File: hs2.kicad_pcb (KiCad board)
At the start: 2 copper layers, 70 x 85 mm, 88 parts, among them J1 Conn_01x01, J2 Conn_01x01, J3 Conn_01x02, Q1 2N5457, Q2 2N3904, Q3 2N3906, Q4 2N3904, U1 Opamp_Dual, U2 Opamp_Dual, U3 Opamp_Dual

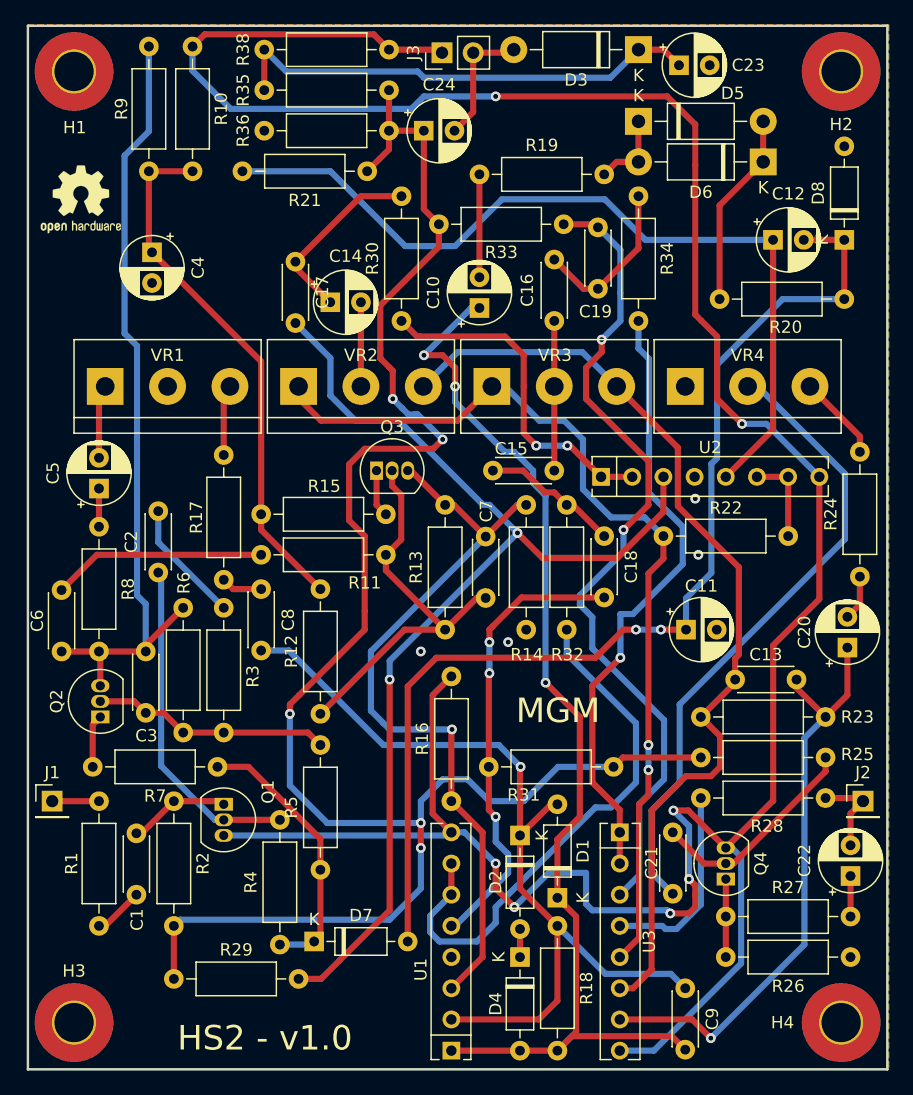
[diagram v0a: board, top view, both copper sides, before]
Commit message: layout: Fixing DRC warnings
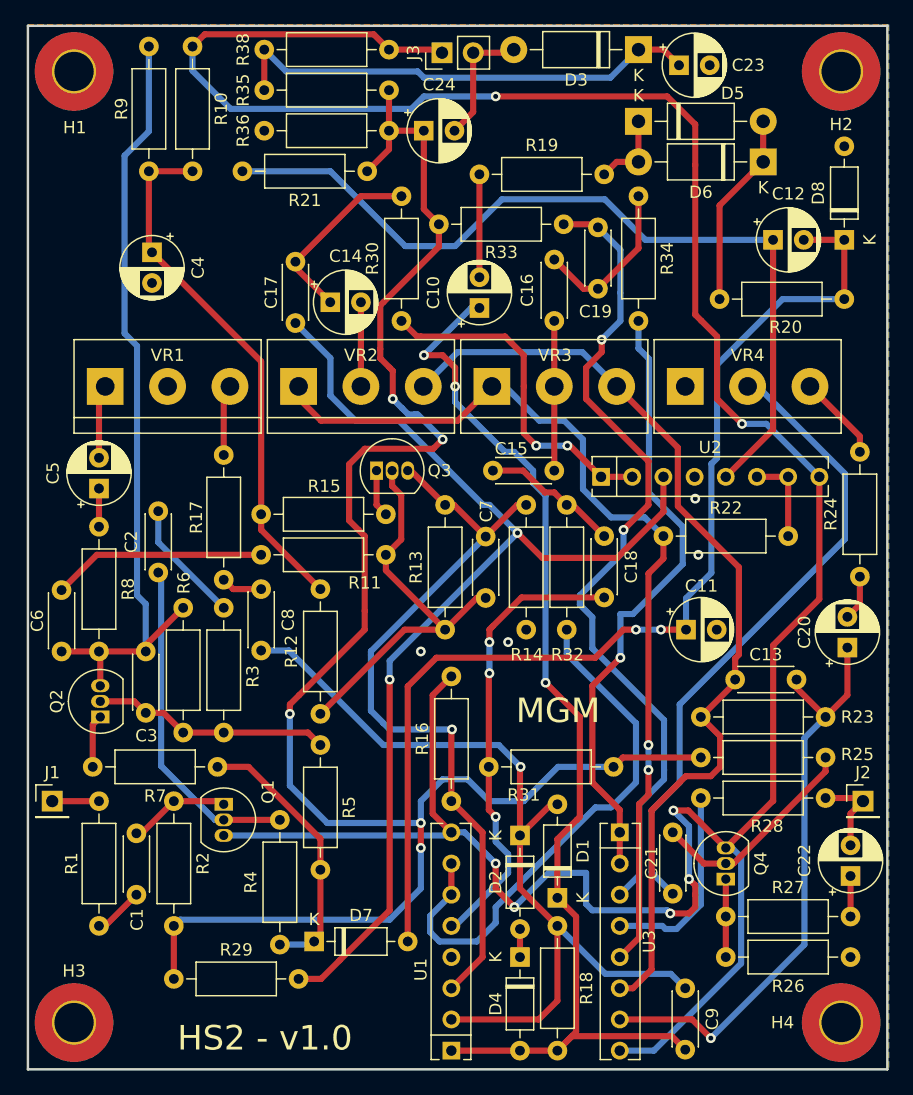
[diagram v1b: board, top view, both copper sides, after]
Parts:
- removed REF**: OSHW-Logo2_7.3x6mm_SilkScreen, Symbol:OSHW-Logo2_7.3x6mm_SilkScreen

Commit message: Minor improvements
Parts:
- added J4: Conn_01x01, Connector_PinHeader_2.54mm:PinHeader_1x01_P2.54mm_Vertical, F.Cu at (103.6, 124.5)
- added J5: Conn_01x01, Connector_PinHeader_2.54mm:PinHeader_1x01_P2.54mm_Vertical, F.Cu at (146.8, 59.2)
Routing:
- net +9V: track 232.0 -> 234.5 mm
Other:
- board text added: "1"
- board text added: "3"
- board text added: "HS2 v1.0"
- board text added: "Input"
- board text added: "Output"
- board text removed: "HS2 - v1.0"
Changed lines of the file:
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@@
     )
   )
+  (footprint "Connector_PinHeader_2.54mm:PinHeader_1x01_P2.54mm_Vertical" (layer "F.Cu")
+    (at 103.632 124.46)
+    (descr "Through hole straight pin header, 1x01, 2.54mm pitch, single row")
+    (tags "Through hole pin header THT 1x01 2.54mm single row")
+    (property "Sheetfile" "hs2.kicad_sch")
+    (property "Sheetname" "")
+    (attr through_hole)
+    (fp_text reference "J4" (at 0 -2.33) (layer "F.SilkS")
+      (effects (font (size 1 1) (thickness 0.15)))
+    )
+    (fp_text value "Conn_01x01" (at 0 2.33) (layer "F.Fab")
+      (effects (font (size 1 1) (thickness 0.15)))
+    )
+    (fp_text user "${REFERENCE}" (at 0 0 90) (layer "F.Fab")
+      (effects (font (size 1 1) (thickness 0.15)))
+    )
+    (fp_line (start -1.33 -1.33) (end 0 -1.33) (layer "F.SilkS") (width 0.12))
+    (fp_line (start -1.33 1.27) (end -1.33 1.33) (layer "F.SilkS") (width 0.12))
+    (fp_line (start -1.33 1.33) (end 1.33 1.33) (layer "F.SilkS") (width 0.12))
+    (fp_line (start 1.33 1.27) (end 1.33 1.33) (layer "F.SilkS") (width 0.12))
+    (fp_line (start -1.33 1.27) (end 1.33 1.27) (layer "F.SilkS") (width 0.12))
+    (fp_line (start -1.33 0) (end -1.33 -1.33) (layer "F.SilkS") (width 0.12))
+    (fp_line (start -1.8 -1.8) (end -1.8 1.8) (layer "F.CrtYd") (width 0.05))
+    (fp_line (start 1.8 -1.8) (end -1.8 -1.8) (layer "F.CrtYd") (width 0.05))
+    (fp_line (start 1.8 1.8) (end 1.8 -1.8) (layer "F.CrtYd") (width 0.05))
+    (fp_line (start -1.8 1.8) (end 1.8 1.8) (layer "F.CrtYd") (width 0.05))
+    (fp_line (start 1.27 -1.27) (end 1.27 1.27) (layer "F.Fab") (width 0.1))
+    (fp_line (start -1.27 -0.635) (end -0.635 -1.27) (layer "F.Fab") (width 0.1))
+    (fp_line (start -1.27 1.27) (end -1.27 -0.635) (layer "F.Fab") (width 0.1))
+    (fp_line (start 1.27 1.27) (end -1.27 1.27) (layer "F.Fab") (width 0.1))
+    (fp_line (start -0.635 -1.27) (end 1.27 -1.27) (layer "F.Fab") (width 0.1))
+    (pad "1" thru_hole rect (at 0 0) (size 1.7 1.7) (drill 1) (layers *.Cu *.Mask)
+      (net 8 "GND") (pinfunction "Pin_1") (pintype "passive"))
+    (model "${KICAD6_3DMODEL_DIR}/Connector_PinHeader_2.54mm.3dshapes/PinHeader_1x01_P2.54mm_Vertical.wrl"
+      (offset (xyz 0 0 0))
+      (scale (xyz 1 1 1))
+      (rotate (xyz 0 0 0))
+    )
+  )
   (footprint "Package_TO_SOT_THT:TO-92_Inline" (layer "F.Cu")
     (at 117.55 114.3 -90)
@@
     )
   )
+  (footprint "Connector_PinHeader_2.54mm:PinHeader_1x01_P2.54mm_Vertical" (layer "F.Cu")
+    (at 146.812 59.182)
+    (descr "Through hole straight pin header, 1x01, 2.54mm pitch, single row")
+    (tags "Through hole pin header THT 1x01 2.54mm single row")
+    (property "Sheetfile" "hs2.kicad_sch")
+    (property "Sheetname" "")
+    (attr through_hole)
+    (fp_text reference "J5" (at -2.794 -0.762) (layer "F.SilkS")
+      (effects (font (size 1 1) (thickness 0.15)))
+    )
+    (fp_text value "Conn_01x01" (at 0 2.33) (layer "F.Fab")
+      (effects (font (size 1 1) (thickness 0.15)))
+    )
+    (fp_text user "${REFERENCE}" (at 0 0 90) (layer "F.Fab")
+      (effects (font (size 1 1) (thickness 0.15)))
+    )
+    (fp_line (start -1.33 1.27) (end -1.33 1.33) (layer "F.SilkS") (width 0.12))
+    (fp_line (start -1.33 0) (end -1.33 -1.33) (layer "F.SilkS") (width 0.12))
+    (fp_line (start -1.33 1.33) (end 1.33 1.33) (layer "F.SilkS") (width 0.12))
+    (fp_line (start 1.33 1.27) (end 1.33 1.33) (layer "F.SilkS") (width 0.12))
+    (fp_line (start -1.33 -1.33) (end 0 -1.33) (layer "F.SilkS") (width 0.12))
+    (fp_line (start -1.33 1.27) (end 1.33 1.27) (layer "F.SilkS") (width 0.12))
+    (fp_line (start -1.8 -1.8) (end -1.8 1.8) (layer "F.CrtYd") (width 0.05))
+    (fp_line (start 1.8 1.8) (end 1.8 -1.8) (layer "F.CrtYd") (width 0.05))
+    (fp_line (start 1.8 -1.8) (end -1.8 -1.8) (layer "F.CrtYd") (width 0.05))
+    (fp_line (start -1.8 1.8) (end 1.8 1.8) (layer "F.CrtYd") (width 0.05))
+    (fp_line (start -1.27 1.27) (end -1.27 -0.635) (layer "F.Fab") (width 0.1))
+    (fp_line (start 1.27 1.27) (end -1.27 1.27) (layer "F.Fab") (width 0.1))
+    (fp_line (start -1.27 -0.635) (end -0.635 -1.27) (layer "F.Fab") (width 0.1))
+    (fp_line (start 1.27 -1.27) (end 1.27 1.27) (layer "F.Fab") (width 0.1))
+    (fp_line (start -0.635 -1.27) (end 1.27 -1.27) (layer "F.Fab") (width 0.1))
+    (pad "1" thru_hole rect (at 0 0) (size 1.7 1.7) (drill 1) (layers *.Cu *.Mask)
+      (net 41 "+9V") (pinfunction "Pin_1") (pintype "passive"))
+    (model "${KICAD6_3DMODEL_DIR}/Connector_PinHeader_2.54mm.3dshapes/PinHeader_1x01_P2.54mm_Vertical.wrl"
+      (offset (xyz 0 0 0))
+      (scale (xyz 1 1 1))
+      (rotate (xyz 0 0 0))
+    )
+  )
   (footprint "TerminalBlock:TerminalBlock_bornier-3_P5.08mm" (layer "F.Cu")
     (at 123.646 80.264)
@@
   )
   (gr_rect (start 101.6 135.89) (end 171.6 50.89) (layer "Edge.Cuts") (width 0.2) (fill none))
-  (gr_text "HS2 - v1.0" (at 120.904 133.35) (layer "F.SilkS")
+  (gr_text "Output" (at 169.672 108.458 90) (layer "B.SilkS")
+    (effects (font (size 1.5 1.5) (thickness 0.3)) (justify mirror))
+  )
+  (gr_text "3" (at 165.354 77.724) (layer "F.SilkS")
+    (effects (font (size 1.5 1.5) (thickness 0.3)))
+  )
+  (gr_text "3" (at 132.588 77.724) (layer "F.SilkS")
+    (effects (font (size 1.5 1.5) (thickness 0.3)))
+  )
+  (gr_text "1" (at 107.95 77.724) (layer "F.SilkS")
+    (effects (font (size 1.5 1.5) (thickness 0.3)))
+  )
+  (gr_text "HS2 v1.0" (at 120.904 133.35) (layer "F.SilkS")
     (effects (font (size 2 2) (thickness 0.3)))
   )
+  (gr_text "1" (at 139.446 77.724) (layer "F.SilkS")
+    (effects (font (size 1.5 1.5) (thickness 0.3)))
+  )
+  (gr_text "3" (at 149.606 77.724) (layer "F.SilkS")
+    (effects (font (size 1.5 1.5) (thickness 0.3)))
+  )
+  (gr_text "1" (at 155.194 77.724) (layer "F.SilkS")
+    (effects (font (size 1.5 1.5) (thickness 0.3)))
+  )
+  (gr_text "1" (at 123.698 77.724) (layer "F.SilkS")
+    (effects (font (size 1.5 1.5) (thickness 0.3)))
+  )
   (gr_text "MGM" (at 144.78 106.68) (layer "F.SilkS")
     (effects (font (size 2 2) (thickness 0.3)))
   )
+  (gr_text "Input" (at 103.632 118.364 270) (layer "F.SilkS")
+    (effects (font (size 1.5 1.5) (thickness 0.3)))
+  )
+  (gr_text "3" (at 118.11 77.724) (layer "F.SilkS")
+    (effects (font (size 1.5 1.5) (thickness 0.3)))
+  )
   (segment (start 107.39 124.206) (end 107.898 124.206) (width 0.5) (layer "F.Cu") (net 1))
   (segment (start 107.898 124.206) (end 110.438 121.666) (width 0.5) (layer "F.Cu") (net 1))
@@
   (segment (start 103.58 114.046) (end 107.39 114.046) (width 0.5) (layer "F.Cu") (net 40))
   (segment (start 155.956 58.928) (end 153.67 56.642) (width 0.5) (layer "F.Cu") (net 41))
+  (segment (start 146.812 59.182) (end 146.812 56.642) (width 0.5) (layer "F.Cu") (net 41))
   (segment (start 131.012 52.832) (end 135.076 52.832) (width 0.5) (layer "F.Cu") (net 41))
   (segment (start 135.076 52.832) (end 135.33 53.086) (width 0.5) (layer "F.Cu") (net 41))
@@
   (segment (start 115.01 52.578) (end 116.006 51.582) (width 0.5) (layer "F.Cu") (net 41))
   (segment (start 159.766 83.312) (end 157.734 81.28) (width 0.5) (layer "F.Cu") (net 41))
-  (segment (start 153.67 56.642) (end 139.7 56.642) (width 0.5) (layer "F.Cu") (net 41))
   (segment (start 139.7 119.126) (end 139.7 121.158) (width 0.5) (layer "F.Cu") (net 41))
   (segment (start 155.956 120.904) (end 155.956 121.666) (width 0.5) (layer "F.Cu") (net 41))
@@
   (segment (start 134.568 105.41) (end 134.568 115.062) (width 0.5) (layer "F.Cu") (net 41))
   (segment (start 155.448 120.396) (end 155.956 120.904) (width 0.5) (layer "F.Cu") (net 41))
+  (segment (start 146.812 56.642) (end 139.7 56.642) (width 0.5) (layer "F.Cu") (net 41))
+  (segment (start 153.67 56.642) (end 146.812 56.642) (width 0.5) (layer "F.Cu") (net 41))
   (segment (start 155.956 62.23) (end 155.956 58.928) (width 0.5) (layer "F.Cu") (net 41))
   (segment (start 134.568 115.062) (end 136.092 116.586) (width 0.5) (layer "F.Cu") (net 41))

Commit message: Minor fixes in the schematics
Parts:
- added REF**: OSHW-Logo2_7.3x6mm_SilkScreen, Symbol:OSHW-Logo2_7.3x6mm_SilkScreen, F.Cu at (106.2, 64.8)
- C13: value 470p -> 470pF
- C21: value 47n -> 47nF
- D5, D6: value DIODE -> 1N34A
- U1, U2, U3: value Opamp_Dual -> M5218L
